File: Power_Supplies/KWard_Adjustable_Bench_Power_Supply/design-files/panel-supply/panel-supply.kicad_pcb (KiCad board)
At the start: 2 copper layers, 63.5 x 39.4 mm, 17 parts, among them J1 12.6VAC input, J2 12V DC fan, J3 B+ voltage meter, J4 B+ current meter, J5 C- voltage meter, U1 LM2940, U2 MEE1S12xxDC, U3 MEE1S12xxDC, U4 MEE1S12xxDC

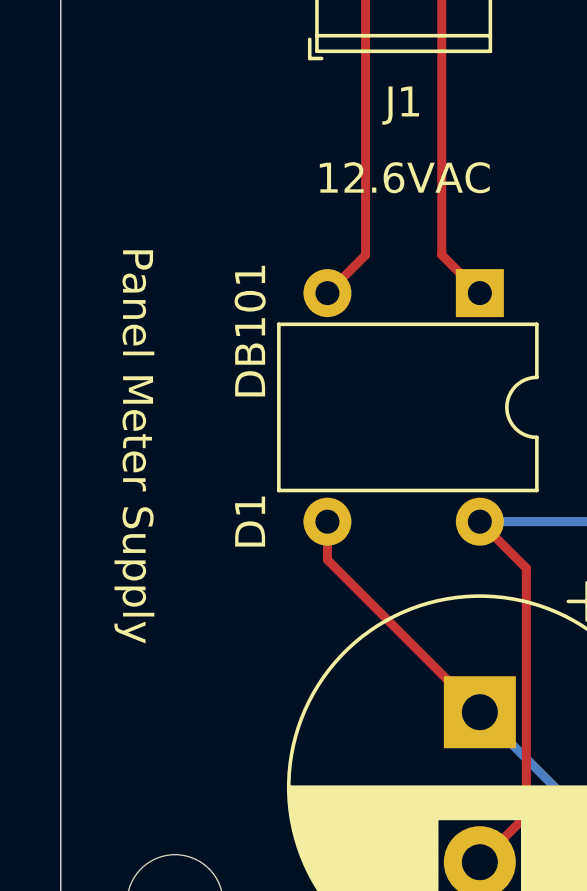
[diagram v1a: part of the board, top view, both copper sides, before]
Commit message: Add board revsion (still 1.0) to the PCB silk screen.
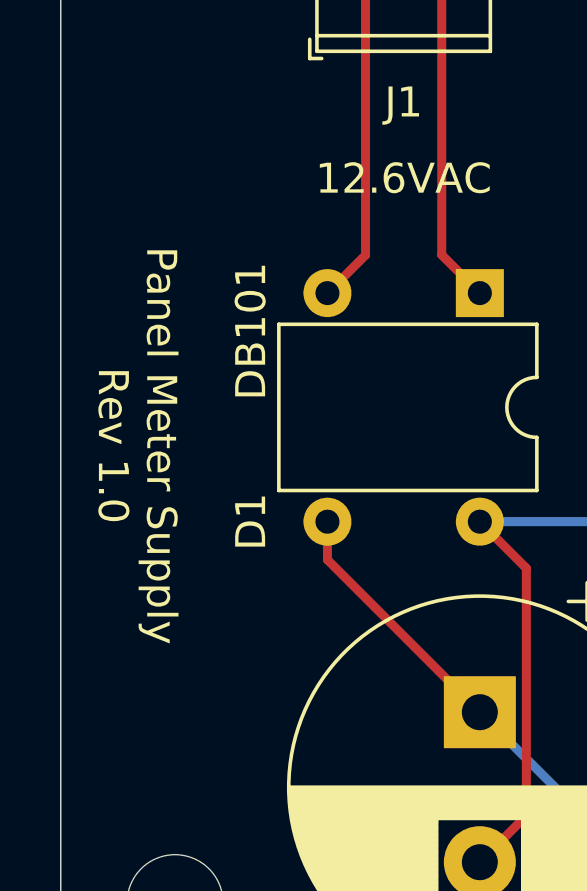
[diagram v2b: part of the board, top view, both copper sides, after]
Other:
- board text added: "Panel Meter Supply Rev 1.0"
- board text removed: "Panel Meter Supply"
